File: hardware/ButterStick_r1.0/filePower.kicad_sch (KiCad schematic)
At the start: 68 parts, among them J7 Conn_01x02_Male, Q4 Q_NMOS_GSD, U10 TLV62569DRL, U16 TLV75801PDRV, U17 TLV75801PDRV, U18 TPS2121, U19 LM74700, U6 TLV62569DRL, U7 TLV62569DRL, U8 TLV62569DRL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

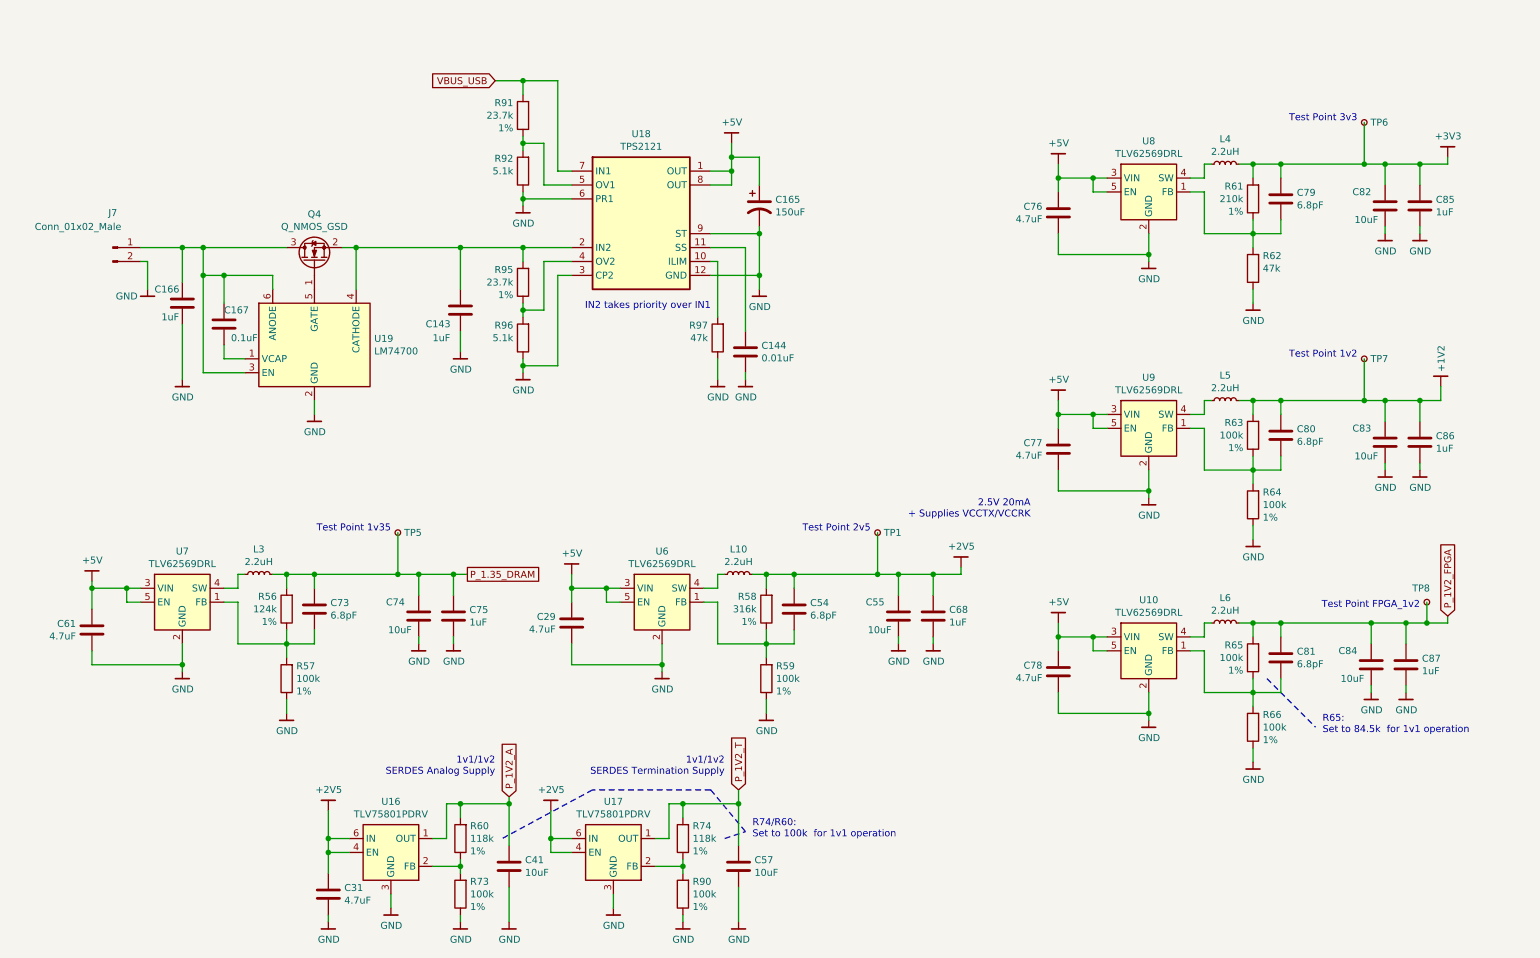
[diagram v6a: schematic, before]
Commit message: Fix RGB G/B signals
- Corrects a mistake where blue and green signals were swapped
- Regenerate schematic

Closes #12
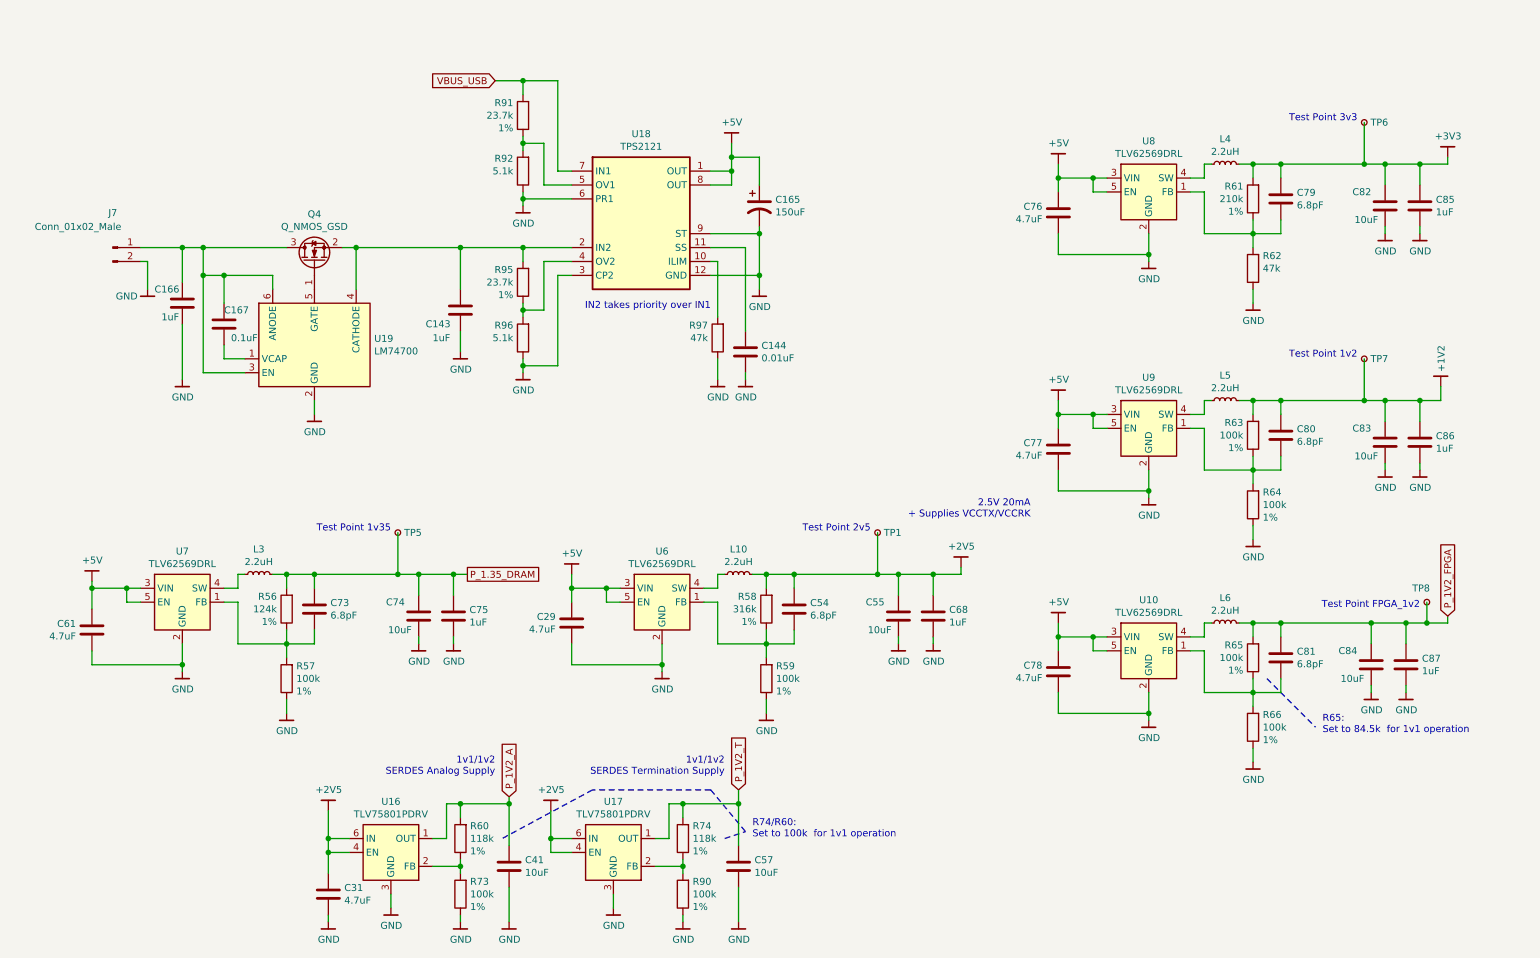
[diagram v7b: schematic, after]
